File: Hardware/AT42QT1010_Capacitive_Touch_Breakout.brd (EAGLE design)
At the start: 25.4 x 33 mm, 28 parts, among them Q1 NPN, U1 AT42QT1010SOT23

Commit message: Ready for red board review
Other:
- board text added: "v10"
- board text removed: "v02"
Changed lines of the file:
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@@
 <setting verticaltext="up"/>
 </settings>
-<grid distance="0.01" unitdist="inch" unit="inch" style="dots" multiple="1" display="yes" altdistance="0.005" altunitdist="inch" altunit="inch"/>
+<grid distance="0.05" unitdist="inch" unit="inch" style="dots" multiple="1" display="yes" altdistance="0.005" altunitdist="inch" altunit="inch"/>
 <layers>
 <layer number="1" name="Top" color="4" fill="1" visible="yes" active="yes"/>
-<layer number="2" name="Route2" color="1" fill="3" visible="yes" active="yes"/>
-<layer number="15" name="Route15" color="4" fill="6" visible="yes" active="yes"/>
+<layer number="2" name="Route2" color="1" fill="3" visible="no" active="yes"/>
+<layer number="15" name="Route15" color="4" fill="6" visible="no" active="yes"/>
 <layer number="16" name="Bottom" color="1" fill="1" visible="yes" active="yes"/>
 <layer number="17" name="Pads" color="2" fill="1" visible="yes" active="yes"/>
@@
 <layer number="23" name="tOrigins" color="15" fill="1" visible="yes" active="yes"/>
 <layer number="24" name="bOrigins" color="15" fill="1" visible="yes" active="yes"/>
-<layer number="25" name="tNames" color="7" fill="1" visible="yes" active="yes"/>
-<layer number="26" name="bNames" color="7" fill="1" visible="yes" active="yes"/>
-<layer number="27" name="tValues" color="7" fill="1" visible="yes" active="yes"/>
-<layer number="28" name="bValues" color="7" fill="1" visible="yes" active="yes"/>
-<layer number="29" name="tStop" color="7" fill="3" visible="yes" active="yes"/>
-<layer number="30" name="bStop" color="7" fill="6" visible="yes" active="yes"/>
-<layer number="31" name="tCream" color="7" fill="4" visible="yes" active="yes"/>
-<layer number="32" name="bCream" color="7" fill="5" visible="yes" active="yes"/>
-<layer number="39" name="tKeepout" color="4" fill="11" visible="yes" active="yes"/>
-<layer number="40" name="bKeepout" color="1" fill="11" visible="yes" active="yes"/>
-<layer number="41" name="tRestrict" color="4" fill="10" visible="yes" active="yes"/>
-<layer number="42" name="bRestrict" color="1" fill="10" visible="yes" active="yes"/>
-<layer number="43" name="vRestrict" color="2" fill="10" visible="yes" active="yes"/>
-<layer number="44" name="Drills" color="7" fill="1" visible="yes" active="yes"/>
+<layer number="25" name="tNames" color="7" fill="1" visible="no" active="yes"/>
+<layer number="26" name="bNames" color="7" fill="1" visible="no" active="yes"/>
+<layer number="27" name="tValues" color="7" fill="1" visible="no" active="yes"/>
+<layer number="28" name="bValues" color="7" fill="1" visible="no" active="yes"/>
+<layer number="29" name="tStop" color="7" fill="3" visible="no" active="yes"/>
+<layer number="30" name="bStop" color="7" fill="6" visible="no" active="yes"/>
+<layer number="31" name="tCream" color="7" fill="4" visible="no" active="yes"/>
+<layer number="32" name="bCream" color="7" fill="5" visible="no" active="yes"/>
+<layer number="39" name="tKeepout" color="4" fill="11" visible="no" active="yes"/>
+<layer number="40" name="bKeepout" color="1" fill="11" visible="no" active="yes"/>
+<layer number="41" name="tRestrict" color="4" fill="10" visible="no" active="yes"/>
+<layer number="42" name="bRestrict" color="1" fill="10" visible="no" active="yes"/>
+<layer number="43" name="vRestrict" color="2" fill="10" visible="no" active="yes"/>
+<layer number="44" name="Drills" color="7" fill="1" visible="no" active="yes"/>
 <layer number="45" name="Holes" color="7" fill="1" visible="yes" active="yes"/>
-<layer number="46" name="Milling" color="3" fill="1" visible="yes" active="yes"/>
+<layer number="46" name="Milling" color="3" fill="1" visible="no" active="yes"/>
 <layer number="51" name="tDocu" color="6" fill="1" visible="yes" active="yes"/>
-<layer number="52" name="bDocu" color="7" fill="1" visible="yes" active="yes"/>
+<layer number="52" name="bDocu" color="7" fill="1" visible="no" active="yes"/>
 <layer number="3" name="Route3" color="4" fill="3" visible="no" active="no"/>
 <layer number="4" name="Route4" color="1" fill="4" visible="no" active="no"/>
@@
 <text x="13.97" y="5.08" size="1.016" layer="22" font="vector" ratio="19" rot="MR270" align="center-right">OUT</text>
 <text x="16.51" y="5.08" size="1.016" layer="22" font="vector" ratio="19" rot="MR270" align="center-right">GND</text>
-<text x="1.27" y="22.86" size="1.2192" layer="1" font="vector" ratio="15" rot="R270" align="center">v02</text>
+<text x="1.27" y="22.86" size="1.2192" layer="1" font="vector" ratio="15" rot="R270" align="center">v10</text>
 <text x="22.86" y="24.638" size="1.016" layer="22" font="vector" ratio="19" rot="MR270" align="center-right">PAD</text>
 <text x="12.7" y="24.13" size="1.016" layer="21" font="vector" ratio="19" align="bottom-center">AT42QT1010</text>

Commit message: Updated connectors library with 1X04-SMD_LONG. Should be no changes in schematic/layout.
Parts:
- moved FRAME1 2.54 mm to (-15.2, -17.8)
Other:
- board text added: "The 0.09055118 in. (2.3mm) hole is NPTH hole"
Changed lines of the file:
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@@
 <setting verticaltext="up"/>
 </settings>
-<grid distance="0.05" unitdist="inch" unit="inch" style="dots" multiple="1" display="yes" altdistance="0.005" altunitdist="inch" altunit="inch"/>
+<grid distance="0.01" unitdist="inch" unit="inch" style="dots" multiple="1" display="yes" altdistance="0.005" altunitdist="inch" altunit="inch"/>
 <layers>
 <layer number="1" name="Top" color="4" fill="1" visible="yes" active="yes"/>
@@
 <text x="12.7" y="22.86" size="1.016" layer="21" font="vector" ratio="19" align="bottom-center">Capacitive Touch</text>
 <text x="12.7" y="21.59" size="1.016" layer="21" font="vector" ratio="19" align="bottom-center">Breakout</text>
-<text x="15.24" y="-15.24" size="1.778" layer="51" ratio="15">Shawn Hymel</text>
+<text x="15.24" y="-17.78" size="1.778" layer="51" ratio="15">Shawn Hymel</text>
 <rectangle x1="0" y1="0" x2="2.54" y2="2.54" layer="41"/>
 <rectangle x1="22.86" y1="0" x2="25.4" y2="2.54" layer="41"/>
@@
 <text x="25.4" y="33.02" size="1.27" layer="51" font="vector" ratio="15">Knock out</text>
 <rectangle x1="18.542" y1="9.398" x2="19.304" y2="10.922" layer="41"/>
+<text x="12.7" y="-7.62" size="1.27" layer="21" font="vector" ratio="15" align="bottom-center">The 0.09055118 in. (2.3mm) hole is NPTH hole</text>
 </plain>
 <attributes>
@@
 <attribute name="VALUE" x="21.5805" y="10.3775" size="0.4064" layer="27" rot="R90"/>
 </element>
-<element name="FRAME1" library="SparkFun-Aesthetics" package="CREATIVE_COMMONS" value="FRAME-LETTER" x="-15.24" y="-15.24"/>
+<element name="FRAME1" library="SparkFun-Aesthetics" package="CREATIVE_COMMONS" value="FRAME-LETTER" x="-15.24" y="-17.78"/>
 <element name="LOGO2" library="SparkFun-Aesthetics" package="OSHW-LOGO-S" value="OSHW-LOGOS" x="22.86" y="19.05" rot="MR0"/>
 <element name="C1" library="SparkFun-Capacitors" package="0603-CAP" value="0.1uF" x="19.05" y="7.62" smashed="yes" rot="R270">

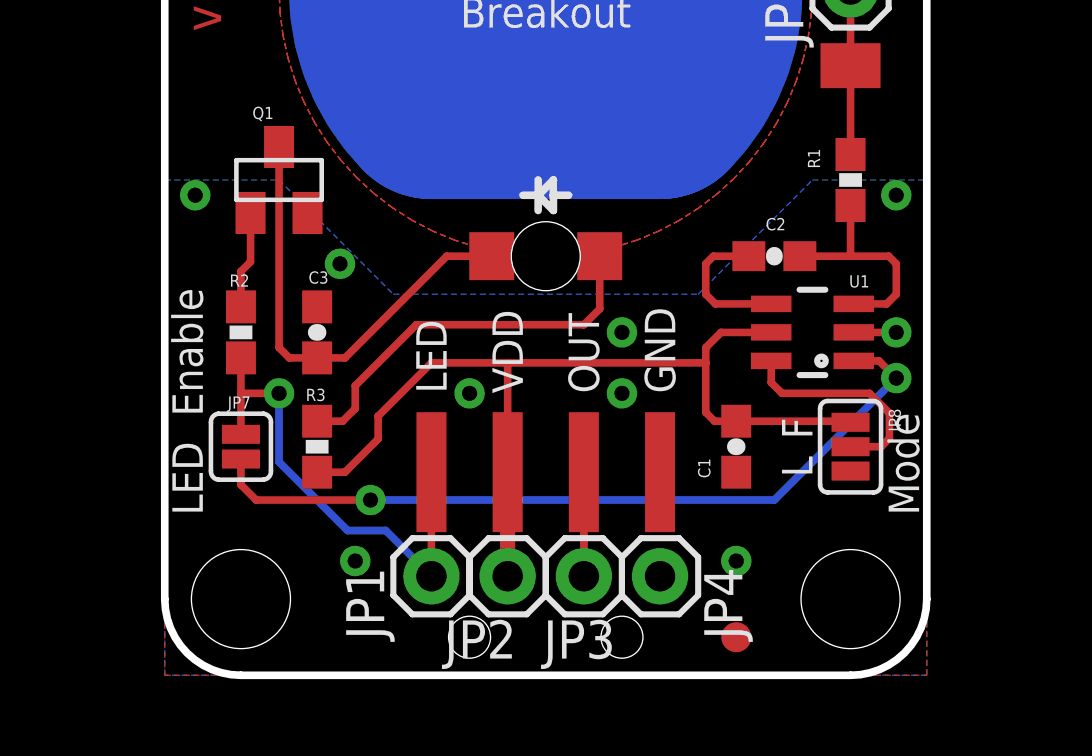
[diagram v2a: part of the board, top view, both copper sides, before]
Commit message: Replaced old IC package with new smaller package
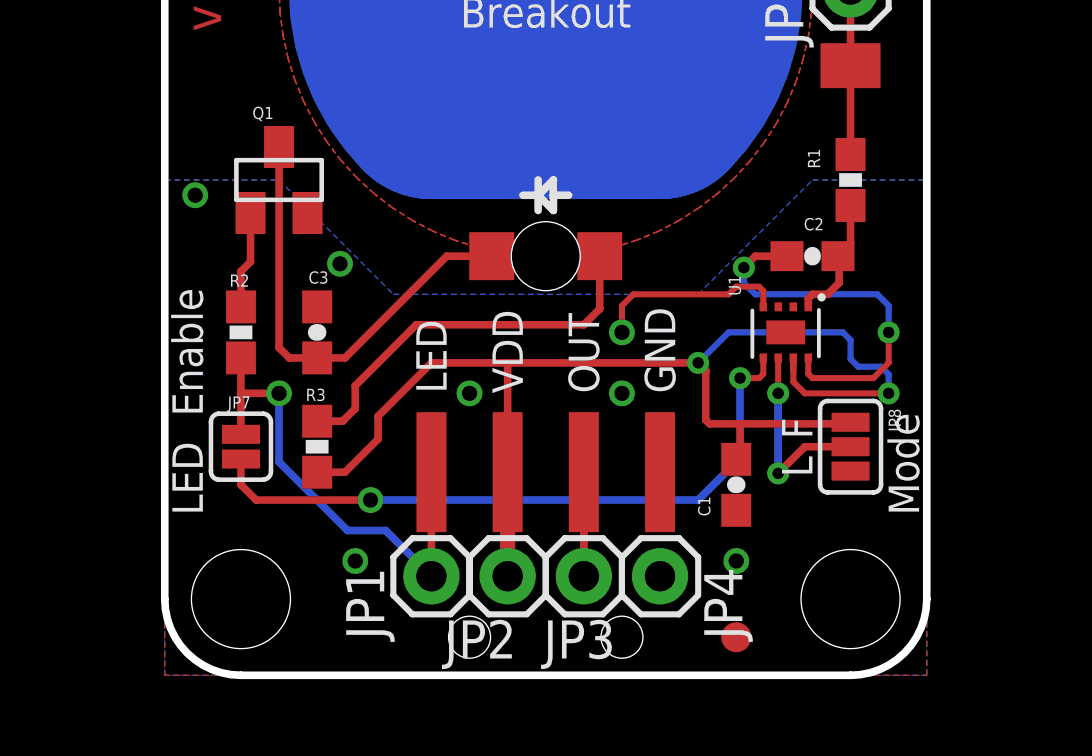
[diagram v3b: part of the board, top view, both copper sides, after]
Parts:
- U1: value AT42QT1010SOT23 -> AT42QT1010UDFN; device SparkFun-DigitalIC:SOT23-6 -> Testing:UDFN/USON_8_PAD
- moved C1 1.27 mm to (19.1, 6.35)
- moved C2 1.27 mm to (21.6, 14.0)
- moved U1 0.89 mm to (20.7, 11.4), turned to 180 degrees
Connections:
- net GND: now also U1.4; no longer U1.2
- net N$4: now also U1.8; no longer U1.4
- net N$5: now also U1.1; no longer U1.3
- net OUT: now also U1.5; no longer U1.1
- net VCC: now also U1.7; no longer U1.5
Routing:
- net VCC: track 31.5 -> 42.9 mm, vias 0 -> 2
- net N$4: track 4.87 -> 12.6 mm, vias 0 -> 2
- net GND: track 1.42 -> 6.45 mm, vias 9 -> 7
- net OUT: track 32.3 -> 28.3 mm
- net N$5: track 7.58 -> 4.29 mm
- net N$7: track 7.34 -> 6.63 mm, vias 0 -> 2

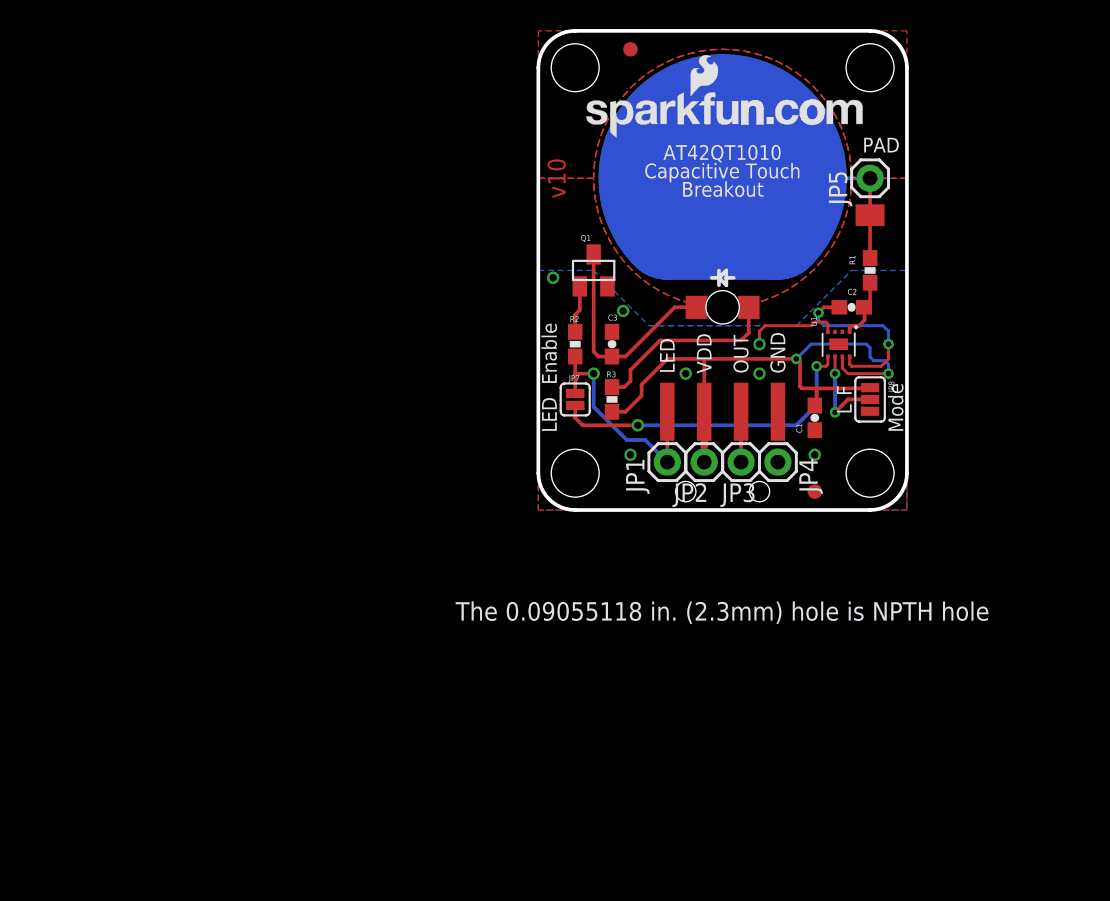
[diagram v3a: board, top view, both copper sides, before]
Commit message: Orphans, Schematic changes
Adjusted some traces, updated CC frame, added VCC range, updated jumpers
to a more current package, added fiducials to underside, added Sparkfun
label to schematic.
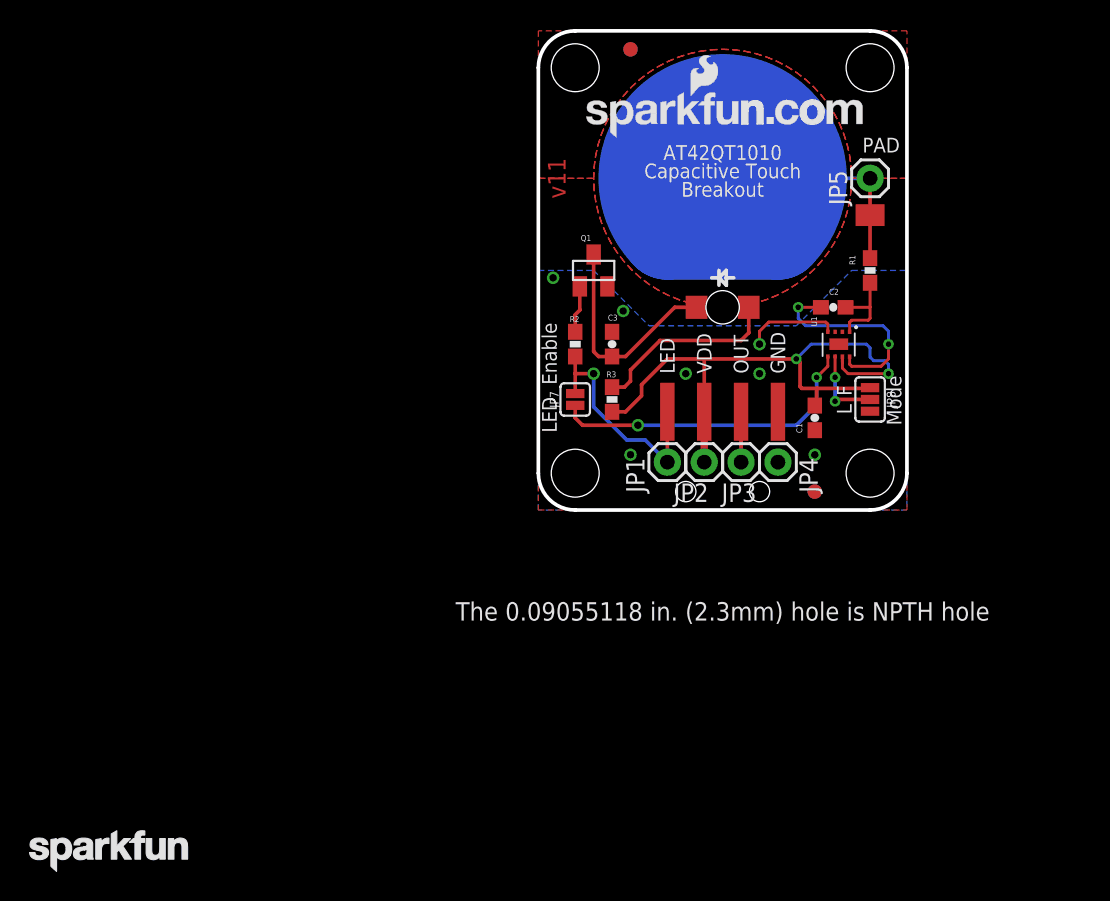
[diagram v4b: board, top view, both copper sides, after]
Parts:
- added FID3, FID4: FIDUCIAL1X2, SparkFun-Aesthetics:FIDUCIAL-1X2
- added LOGO4: SFE_LOGO_NAME.1_INCH, SparkFun-Aesthetics:SFE_LOGO_NAME_.1
- JP7: value NC -> JUMPER-SMT_2_NO_SILK; device SparkFun-Passives:SJ_2S -> SparkFun-Jumpers:SMT-JUMPER_2_NO_SILK
- JP8: value JUMPER-31-2 -> JUMPER-SMT_3_NO_SILK; device SparkFun-Passives:SJ_3_PASTE1&2 -> SparkFun-Jumpers:SMT-JUMPER_3_NO_SILK
- moved C2 1.27 mm to (20.3, 14.0)
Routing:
- net N$5: track 4.29 -> 6.32 mm
- net N$4: track 12.6 -> 14.4 mm
- net N$7: track 6.63 -> 5.55 mm
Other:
- board text added: "Elias Santistevan"
- board text added: "Revised by:"
- board text added: "v11"
- board text removed: "v10"
